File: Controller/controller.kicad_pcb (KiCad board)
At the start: 2 copper layers, 108.3 x 63.7 mm, 7 parts, among them SW1 SW_Push, SW2 SW_Push, SW3 SW_Push, U1 XIAO-RP2040-DIP, U2 COM-09032, U3 COM-09032

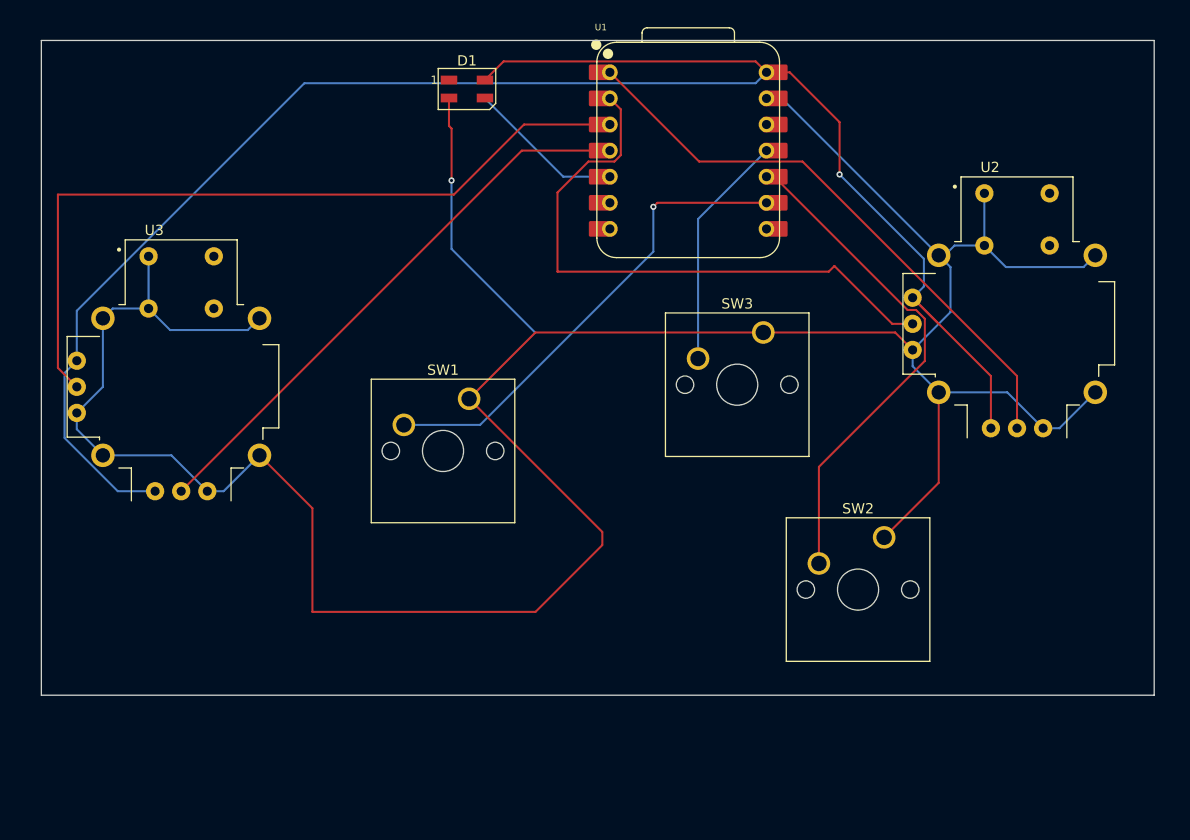
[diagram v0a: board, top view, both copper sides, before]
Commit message: Connected the GND and set stuff up
Next do the firmware and the case
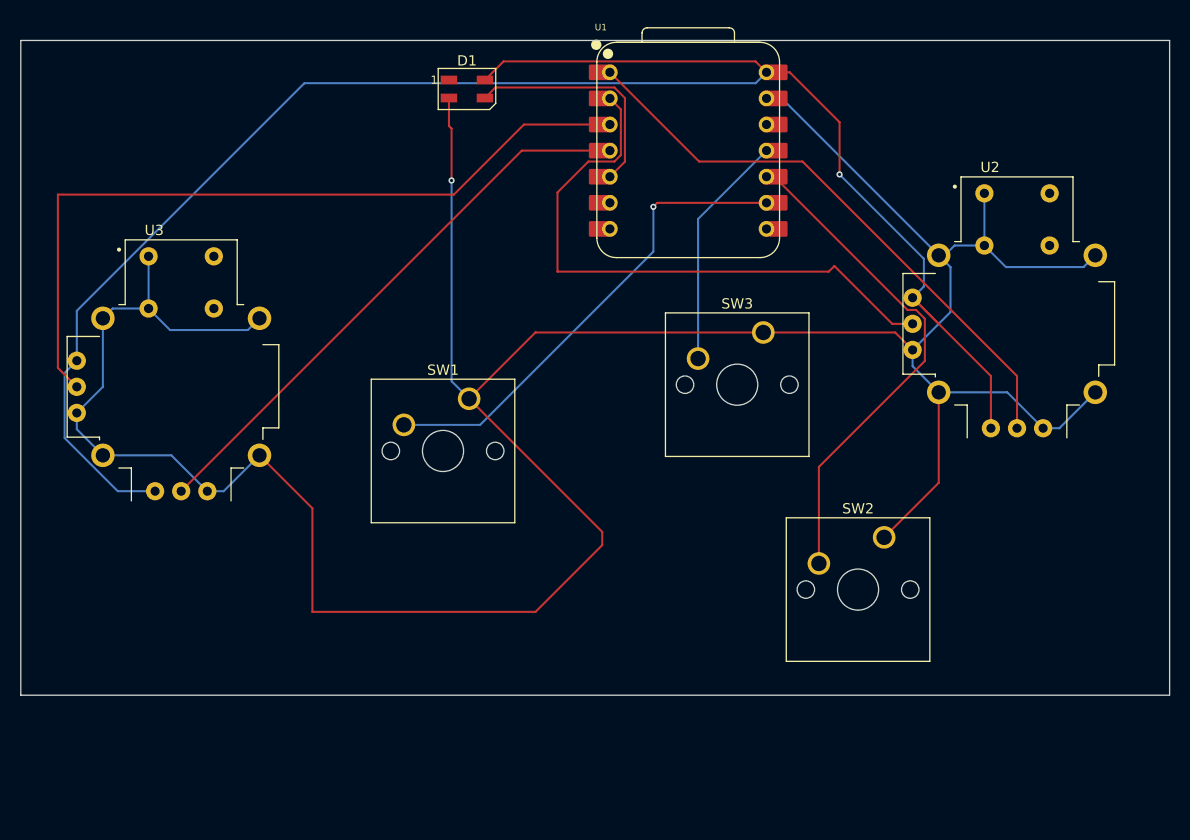
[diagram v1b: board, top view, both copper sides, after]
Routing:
- net Net-(D1-DIN): track 15.3 -> 22.7 mm
- net GND: track 292.4 -> 296.2 mm
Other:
- board size 108.3 x 63.7 mm -> 111.8 x 63.7 mm
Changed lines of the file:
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@@
 	)
 	(gr_rect
-		(start 78.88 41.9)
-		(end 187.18 105.62)
+		(start 76.88 41.9)
+		(end 188.68 105.62)
 		(stroke
 			(width 0.05)
@@
 	)
 	(segment
+		(start 127 70.32)
+		(end 149.14 70.32)
+		(width 0.2)
+		(layer "F.Cu")
+		(net 1)
+	)
+	(segment
 		(start 126.96 70.32)
-		(end 149.14 70.32)
+		(end 127 70.32)
 		(width 0.2)
 		(layer "F.Cu")
@@
 	)
 	(segment
-		(start 118.8 55.53)
-		(end 118.8 62.19)
-		(width 0.2)
-		(layer "B.Cu")
-		(net 1)
-	)
-	(segment
 		(start 181.45 76.145)
 		(end 177.9575 79.6375)
@@
 	)
 	(segment
+		(start 118.8 75.06)
+		(end 120.51 76.77)
+		(width 0.2)
+		(layer "B.Cu")
+		(net 1)
+	)
+	(segment
 		(start 82.33 79.735)
 		(end 84.87 82.275)
@@
 	)
 	(segment
+		(start 118.8 55.53)
+		(end 118.8 75.06)
+		(width 0.2)
+		(layer "B.Cu")
+		(net 1)
+	)
+	(segment
 		(start 166.21 76.145)
 		(end 172.8775 76.145)
@@
 	)
 	(segment
-		(start 118.8 62.19)
-		(end 126.92 70.31)
-		(width 0.2)
-		(layer "B.Cu")
-		(net 1)
-	)
-	(segment
 		(start 166.21 62.81)
 		(end 150.94 47.54)
@@
 	)
 	(segment
-		(start 129.67 55.16)
-		(end 122.05 47.54)
-		(width 0.2)
-		(layer "B.Cu")
+		(start 123.073 46.477)
+		(end 122.05 47.5)
+		(width 0.2)
+		(layer "F.Cu")
 		(net 2)
 	)
 	(segment
+		(start 135.674 47.50069)
+		(end 134.65031 46.477)
+		(width 0.2)
+		(layer "F.Cu")
+		(net 2)
+	)
+	(segment
+		(start 135.674 53.696)
+		(end 135.674 47.50069)
+		(width 0.2)
+		(layer "F.Cu")
+		(net 2)
+	)
+	(segment
 		(start 134.21 55.16)
-		(end 129.67 55.16)
-		(width 0.2)
-		(layer "B.Cu")
+		(end 135.674 53.696)
+		(width 0.2)
+		(layer "F.Cu")
 		(net 2)
 	)
+	(segment
+		(start 134.65031 46.477)
+		(end 123.073 46.477)
+		(width 0.2)
+		(layer "F.Cu")
+		(net 2)
+	)

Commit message: (I think) I finished the firmware for the controller
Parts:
- added SW4: SW_Push, Button_Switch_Keyboard:SW_Cherry_MX_1.00u_PCB, F.Cu at (95.6, 98.6)
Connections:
- U1 pad 8: unconnected-(U1-GPIO1/RX-Pad8) -> Net-(U1-GPIO1/RX)
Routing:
- net Net-(U1-GPIO1/RX): track 0.00 -> 79.3 mm, vias 0 -> 3
- net GND: track 296.2 -> 331.7 mm
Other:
- board size 111.8 x 63.7 mm -> 111.8 x 75.8 mm
